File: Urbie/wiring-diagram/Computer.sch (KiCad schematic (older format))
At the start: 11 parts

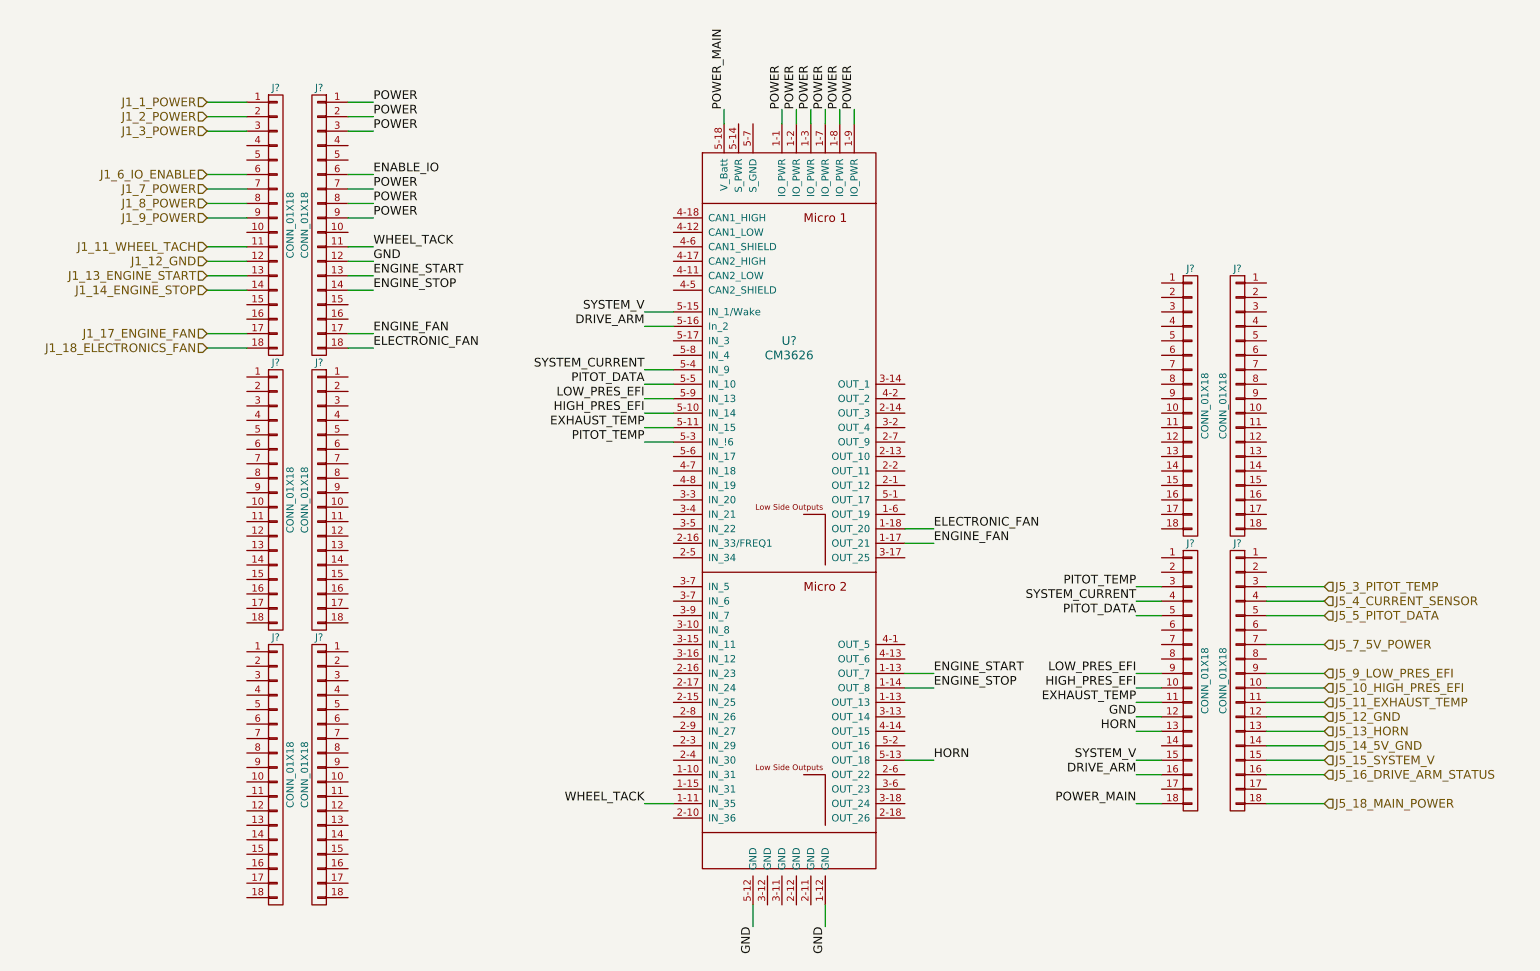
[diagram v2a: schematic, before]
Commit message: Changed computer sheet in Urbie Wiring diagrams
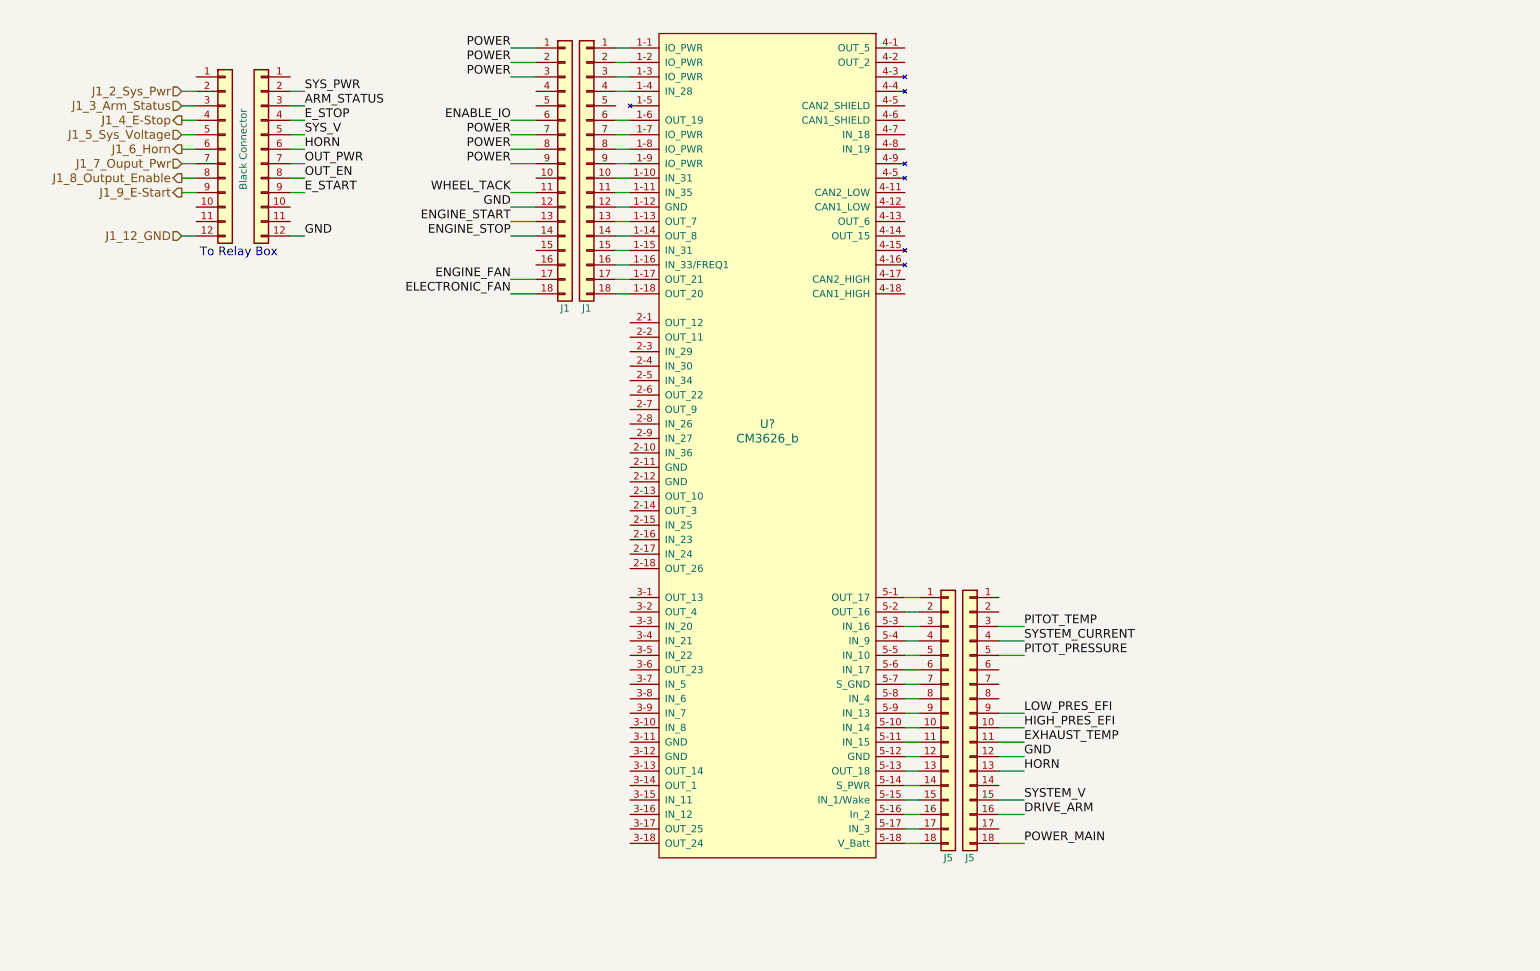
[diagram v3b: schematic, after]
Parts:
- removed J? (x10): CONN_01X18, symbol CONN_01X18
- removed U?: CM3626, symbol CM3626
- added J? (x2): Black Connector, symbol Conn_01x12
- added J? (x2): J1, symbol Conn_01x18
- added J? (x2): J5, symbol Conn_01x18
- added U?: CM3626_b, symbol CM3626_b
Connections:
- net DRIVE_ARM: now also J?.16 (Pin_16)
- net ELECTRONIC_FAN: now also J?.18 (Pin_18)
- net ENABLE_IO: now also J?.6 (Pin_6)
- net ENGINE_FAN: now also J?.17 (Pin_17)
- net ENGINE_START: now also J?.13 (Pin_13)
- net ENGINE_STOP: now also J?.14 (Pin_14)
- net EXHAUST_TEMP: now also J?.11 (Pin_11)
- net GND: now also J?.12 (Pin_12), J?.12 (Pin_12), J?.12 (Pin_12)
- net HIGH_PRES_EFI: now also J?.10 (Pin_10)
- net HORN: now also J?.13 (Pin_13), J?.6 (Pin_6)
- net J1_12_GND: now also J?.12 (Pin_12)
- net LOW_PRES_EFI: now also J?.9 (Pin_9)
- net PITOT_TEMP: now also J?.3 (Pin_3)
- net POWER: now also J?.1 (Pin_1), J?.2 (Pin_2), J?.3 (Pin_3), J?.7 (Pin_7), J?.8 (Pin_8), J?.9 (Pin_9)
- net POWER_MAIN: now also J?.18 (Pin_18)
- net SYSTEM_CURRENT: now also J?.4 (Pin_4)
- net SYSTEM_V: now also J?.15 (Pin_15)
- net WHEEL_TACK: now also J?.11 (Pin_11)
- new net: J?.1 (Pin_1), U?.1-1 (IO_PWR)
- new net: J?.10 (Pin_10), U?.1-10 (IN_31)
- new net: J?.11 (Pin_11), U?.1-11 (IN_35)
- new net: J?.12 (Pin_12), U?.1-12 (GND)
- new net: J?.13 (Pin_13), U?.1-13 (OUT_7)
- new net: J?.14 (Pin_14), U?.1-14 (OUT_8)
- new net: J?.15 (Pin_15), U?.1-15 (IN_31)
- new net: J?.16 (Pin_16), U?.1-16 (IN_33/FREQ1)
- new net: J?.17 (Pin_17), U?.1-17 (OUT_21)
- new net: J?.18 (Pin_18), U?.1-18 (OUT_20)
- new net: J?.2 (Pin_2), U?.1-2 (IO_PWR)
- new net: J?.3 (Pin_3), U?.1-3 (IO_PWR)
- new net: J?.4 (Pin_4), U?.1-4 (IN_28)
- new net: J?.6 (Pin_6), U?.1-6 (OUT_19)
- new net: J?.7 (Pin_7), U?.1-7 (IO_PWR)
- new net: J?.8 (Pin_8), U?.1-8 (IO_PWR)
- new net: J?.9 (Pin_9), U?.1-9 (IO_PWR)
- new net: J?.1 (Pin_1), U?.5-1 (OUT_17)
- new net: J?.10 (Pin_10), U?.5-10 (IN_14)
- new net: J?.11 (Pin_11), U?.5-11 (IN_15)
- new net: J?.12 (Pin_12), U?.5-12 (GND)
- new net: J?.13 (Pin_13), U?.5-13 (OUT_18)
- new net: J?.14 (Pin_14), U?.5-14 (S_PWR)
- new net: J?.15 (Pin_15), U?.5-15 (IN_1/Wake)
- new net: J?.16 (Pin_16), U?.5-16 (In_2)
- new net: J?.17 (Pin_17), U?.5-17 (IN_3)
- new net: J?.18 (Pin_18), U?.5-18 (V_Batt)
- new net: J?.2 (Pin_2), U?.5-2 (OUT_16)
- new net: J?.3 (Pin_3), U?.5-3 (IN_16)
- new net: J?.4 (Pin_4), U?.5-4 (IN_9)
- new net: J?.5 (Pin_5), U?.5-5 (IN_10)
- new net: J?.6 (Pin_6), U?.5-6 (IN_17)
- new net: J?.7 (Pin_7), U?.5-7 (S_GND)
- new net: J?.8 (Pin_8), U?.5-8 (IN_4)
- new net: J?.9 (Pin_9), U?.5-9 (IN_13)
- new net ARM_STATUS: J?.3 (Pin_3)
- new net E_START: J?.9 (Pin_9)
- new net E_STOP: J?.4 (Pin_4)
- new net J1_2_Sys_Pwr: J?.2 (Pin_2)
- new net J1_3_Arm_Status: J?.3 (Pin_3)
- new net J1_4_E-Stop: J?.4 (Pin_4)
- new net J1_5_Sys_Voltage: J?.5 (Pin_5)
- new net J1_6_Horn: J?.6 (Pin_6)
- new net J1_7_Ouput_Pwr: J?.7 (Pin_7)
- new net J1_8_Output_Enable: J?.8 (Pin_8)
- new net J1_9_E-Start: J?.9 (Pin_9)
- new net OUT_EN: J?.8 (Pin_8)
- new net OUT_PWR: J?.7 (Pin_7)
- new net PITOT_PRESSURE: J?.5 (Pin_5)
- new net SYS_PWR: J?.2 (Pin_2)
- new net SYS_V: J?.5 (Pin_5)
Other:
- note added: "To Relay Box"
